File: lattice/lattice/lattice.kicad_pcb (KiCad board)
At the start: 2 copper layers, 286.9 x 128.7 mm, 161 parts, among them J1 AudioJack2, J10 AudioJack2, J11 AudioJack2, J12 AudioJack2, J13 AudioJack2, J14 AudioJack2, J15 AudioJack2, J16 Conn_02x05_Odd_Even, J17 Conn_01x10, J18 Conn_01x10, J19 Conn_01x08, J2 AudioJack2, J20 Conn_01x08, J21 Conn_01x07, J22 Conn_01x07, J23 Conn_01x07, J24 Conn_01x07, J25 Conn_02x05_Odd_Even, J26 AudioJack3, J26 WEEE, J27 Conn_01x03, J27 OSHW, J28 Conn_01x03, J29 AudioJack2, J3 AudioJack2, J30 AudioJack2, J4 AudioJack2, J5 AudioJack2, J6 AudioJack2, J7 AudioJack2, J8 AudioJack2, J9 Conn_02x08_Odd_Even, Q1 BC548, Q2 BC548, SW1 LP4OA1PBCT, U1 MCP6002-xP, U2 MCP6002-xP, U3 MCP6002-xP, U5 6N138, U6 LM4040LP-5, U7 74HC595

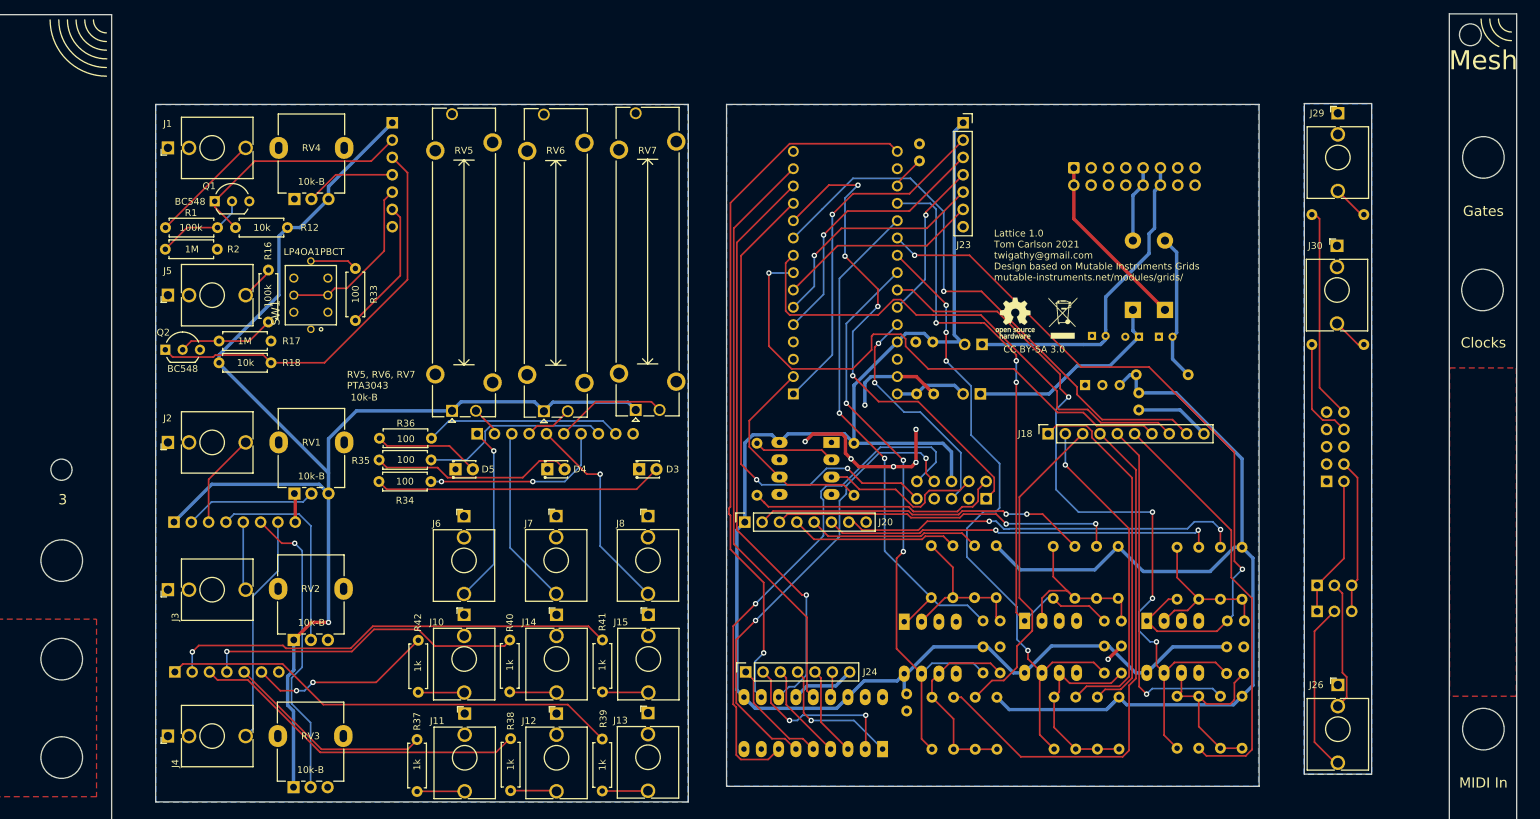
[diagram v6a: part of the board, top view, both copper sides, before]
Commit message: Tweaks and fixes (Lattice)
-DIP-18 to DIP-16
-Rotate one of the electrolytic caps
-Switch silkscreen fix
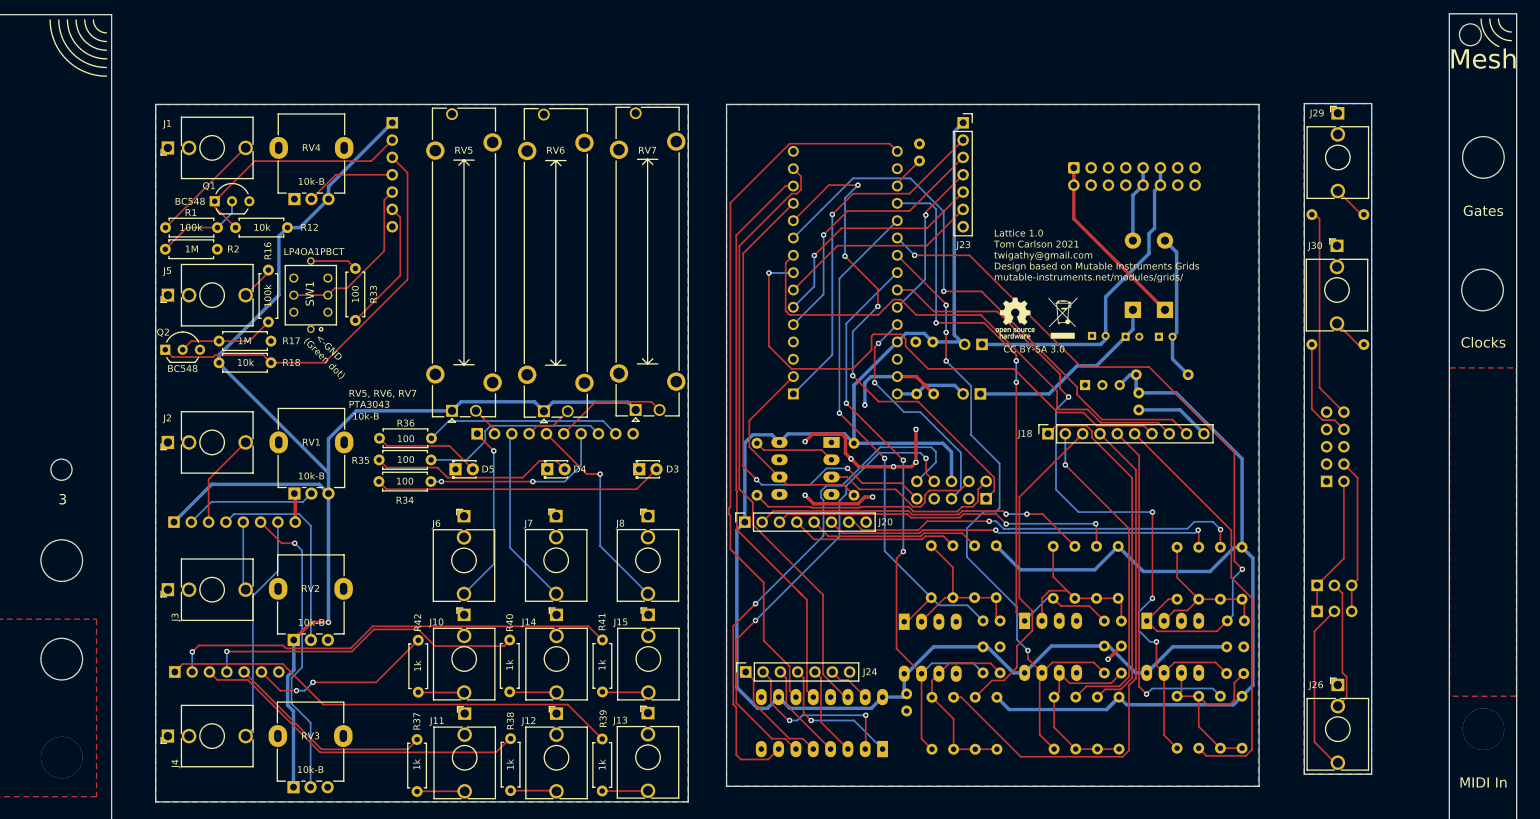
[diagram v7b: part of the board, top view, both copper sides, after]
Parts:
- U7: footprint Package_DIP:DIP-18_W7.62mm_Socket_LongPads -> Package_DIP:DIP-16_W7.62mm_Socket_LongPads
- moved C8 1.96 mm to (207.9, 81.7), turned to 0 degrees
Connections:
- REF** pad : (no net) -> Earth (x2)
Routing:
- net /MOSI: track 85.9 -> 88.9 mm
- net /CH1A: track 31.0 -> 33.5 mm
- net +12V: track 31.0 -> 29.1 mm
- net Earth: track 67.4 -> 68.8 mm, vias 7 -> 9
- net /SCK: track 104.1 -> 105.1 mm, vias 1 -> 0
- net /SS: track 85.1 -> 84.4 mm, vias 1 -> 0
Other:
- board text added: "<-GND (Green dot)"

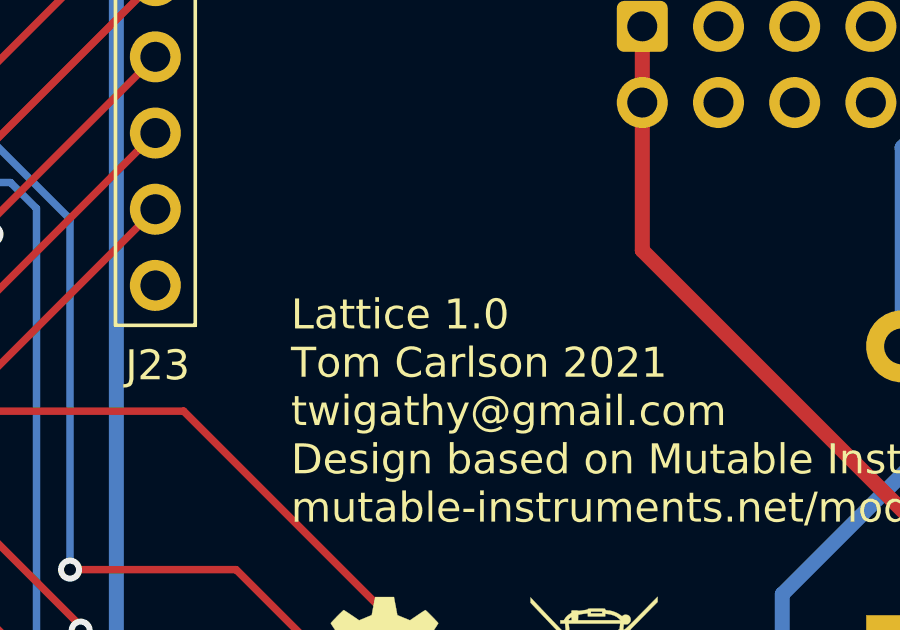
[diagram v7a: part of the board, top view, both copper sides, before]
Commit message: Bumping versions on silkscreens for Lattice
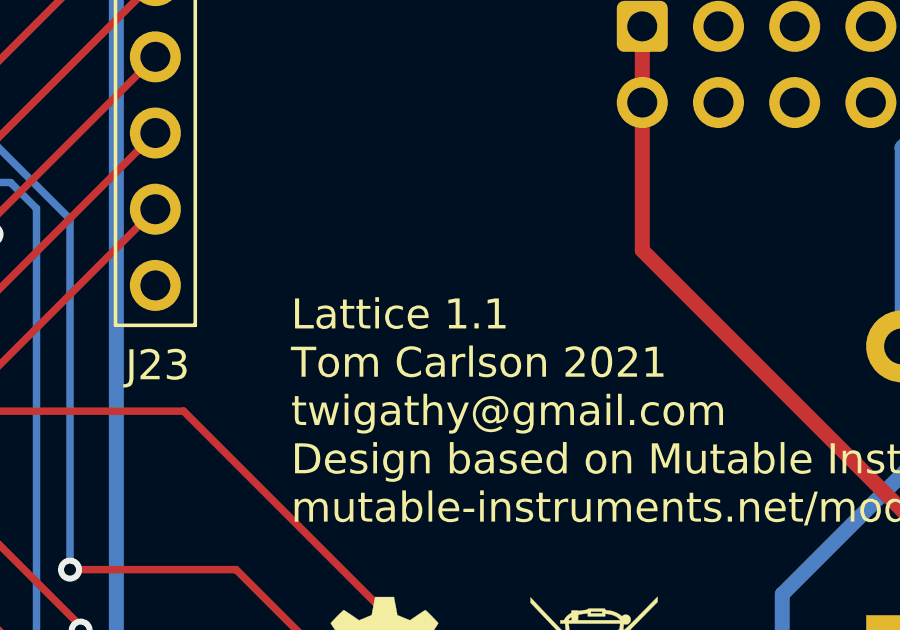
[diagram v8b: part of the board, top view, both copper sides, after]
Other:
- board text added: "Lattice 1.1 Tom Carlson 2021 twigathy@gmail.com Design based on Mutable Instruments Grids mutable-instruments.net/modules/grids/"
- board text removed: "Lattice 1.0 Tom Carlson 2021 twigathy@gmail.com Design based on Mutable Instruments Grids mutable-instruments.net/modules/grids/"
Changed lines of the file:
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@@
   (gr_line (start 243.967 47.4726) (end 234.0964 47.4726) (layer Edge.Cuts) (width 0.05))
   (gr_line (start 234.0964 47.4726) (end 234.0964 145.796) (layer Edge.Cuts) (width 0.05))
-  (gr_text "Lattice 1.0\nTom Carlson 2021\ntwigathy@gmail.com\nDesign based on Mutable Instruments Grids\nmutable-instruments.net/modules/grids/" (at 188.595 69.723) (layer F.SilkS)
+  (gr_text "Lattice 1.1\nTom Carlson 2021\ntwigathy@gmail.com\nDesign based on Mutable Instruments Grids\nmutable-instruments.net/modules/grids/" (at 188.595 69.723) (layer F.SilkS)
     (effects (font (size 1 1) (thickness 0.15)) (justify left))
   )
@@
     (effects (font (size 1 1) (thickness 0.25)))
   )
-  (gr_text "Lattice 1.0\nTom Carlson 2021\ntwigathy@gmail.com\nDesign based on Mutable Instruments Grids\nmutable-instruments.net/modules/grids/" (at 139.573 62.357) (layer B.SilkS)
+  (gr_text "Lattice 1.1\nTom Carlson 2021\ntwigathy@gmail.com\nDesign based on Mutable Instruments Grids\nmutable-instruments.net/modules/grids/" (at 139.573 62.357) (layer B.SilkS)
     (effects (font (size 1 1) (thickness 0.15)) (justify left mirror))
   )
@@
     (effects (font (size 1 1) (thickness 0.25)) (justify mirror))
   )
-  (gr_text "Lattice 1.0\nTom Carlson 2021\ntwigathy@gmail.com\nDesign based on Mutable Instruments Grids\nmutable-instruments.net/modules/grids/" (at 57.277 47.117) (layer B.SilkS)
+  (gr_text "Lattice 1.1\nTom Carlson 2021\ntwigathy@gmail.com\nDesign based on Mutable Instruments Grids\nmutable-instruments.net/modules/grids/" (at 57.277 47.117) (layer B.SilkS)
     (effects (font (size 1 1) (thickness 0.15)) (justify left mirror))
   )
